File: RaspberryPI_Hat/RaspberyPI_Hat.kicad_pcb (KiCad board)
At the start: 2 copper layers, 65 x 56 mm, 43 parts, among them Q1 BC817, Q2 BC817, Q3 BC817, SW1 SW_PUSH, U1 CAT24C32WI-GT3

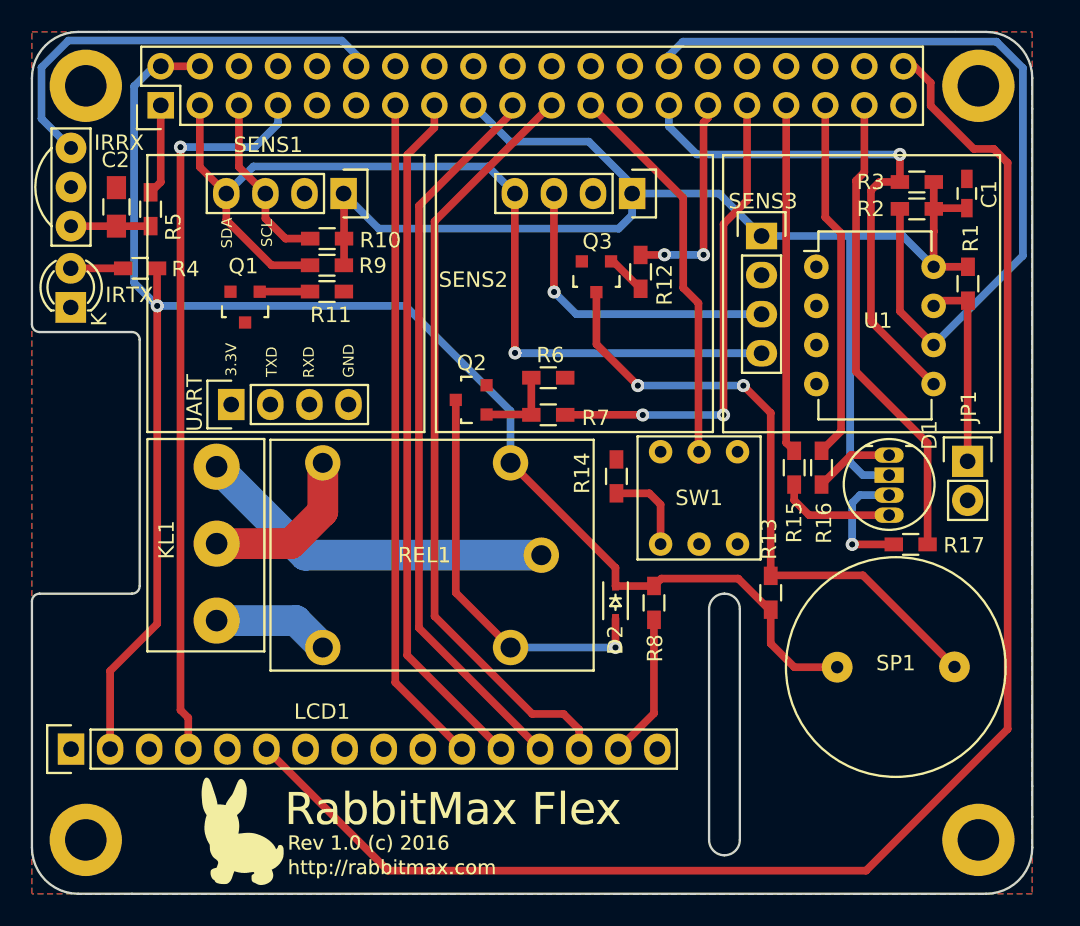
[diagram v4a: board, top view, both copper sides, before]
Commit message: Text on socket's pads
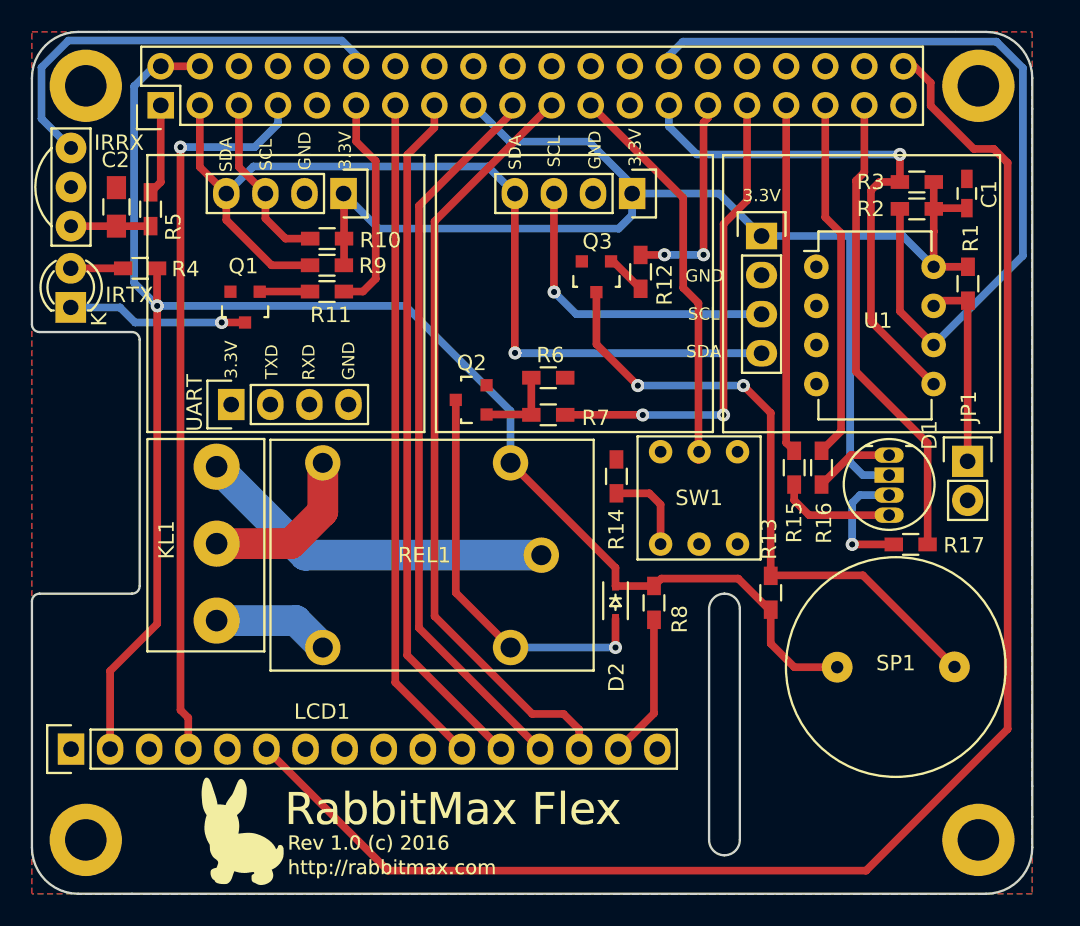
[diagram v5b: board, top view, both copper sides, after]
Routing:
- net Net-(R11-Pad2): track 0.00 -> 14.2 mm
- net Net-(IRTX1-Pad1): track 0.00 -> 11.7 mm, vias 0 -> 1
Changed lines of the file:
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@@
   (general
     (links 102)
-    (no_connects 9)
-    (area 97.924999 68.524999 163.075001 124.675001)
+    (no_connects 7)
+    (area 86.242429 56.842428 174.757572 125.479)
     (thickness 1.6)
-    (drawings 34)
-    (tracks 234)
+    (drawings 44)
+    (tracks 245)
     (zones 0)
     (modules 43)
@@
     (40 Dwgs.User user)
     (41 Cmts.User user)
-    (42 Eco1.User user)
-    (43 Eco2.User user)
+    (42 Eco1.User user hide)
+    (43 Eco2.User user hide)
     (44 Edge.Cuts user)
     (45 Margin user)
@@
     (visible_elements 7FFEEE7F)
     (pcbplotparams
-      (layerselection 0x00030_80000001)
+      (layerselection 0x010e0_80000001)
       (usegerberextensions false)
       (excludeedgelayer true)
@@
     (descr "Through hole pin header")
     (tags "pin header")
-    (fp_text reference SENS2 (at 8.1 15.57 360) (layer F.SilkS)
+    (fp_text reference SENS2 (at 8.1 15.57 360) (layer F.SilkS) hide
       (effects (font (size 1 1) (thickness 0.15)))
     )
@@
     (descr "Through hole pin header")
     (tags "pin header")
-    (fp_text reference SENS1 (at -0.66 10.15 360) (layer F.SilkS)
+    (fp_text reference SENS1 (at -0.66 10.15 360) (layer F.SilkS) hide
       (effects (font (size 1 1) (thickness 0.15)))
     )
@@
     (tags SOD-323)
     (attr smd)
-    (fp_text reference D2 (at 2.45 0.01 270) (layer F.SilkS)
+    (fp_text reference D2 (at 4.87 -0.06 270) (layer F.SilkS)
       (effects (font (size 1 1) (thickness 0.15)))
     )
@@
     (tags "resistor 0603")
     (attr smd)
-    (fp_text reference R8 (at -2.95 0.07 270) (layer F.SilkS)
+    (fp_text reference R8 (at -1.06 1.67 270) (layer F.SilkS)
       (effects (font (size 1 1) (thickness 0.15)))
     )
@@
     (tags "resistor 0603")
     (attr smd)
-    (fp_text reference R14 (at 0.21 -2.23 90) (layer F.SilkS)
+    (fp_text reference R14 (at -3.45 0 90) (layer F.SilkS)
       (effects (font (size 1 1) (thickness 0.15)))
     )
@@
     (descr "Through hole pin header")
     (tags "pin header")
-    (fp_text reference SENS3 (at 2.59 2.99) (layer F.SilkS)
+    (fp_text reference SENS3 (at 2.59 2.99) (layer F.SilkS) hide
       (effects (font (size 1 1) (thickness 0.15)))
     )
@@
     )
   )
-  (gr_text SDA (at 110.67 81.66 90) (layer F.SilkS)
-    (effects (font (size 0.7 0.7) (thickness 0.1)))
-  )
-  (gr_text SCL (at 113.27 81.67 90) (layer F.SilkS)
-    (effects (font (size 0.7 0.7) (thickness 0.1)))
+  (gr_text SCL (at 141.65 86.93) (layer F.SilkS)
+    (effects (font (size 0.8 0.8) (thickness 0.1)))
+  )
+  (gr_text SDA (at 141.65 89.37) (layer F.SilkS)
+    (effects (font (size 0.8 0.8) (thickness 0.1)))
+  )
+  (gr_text SDA (at 129.4 76.42 90) (layer F.SilkS)
+    (effects (font (size 0.8 0.8) (thickness 0.1)))
+  )
+  (gr_text SCL (at 131.93 76.36 90) (layer F.SilkS)
+    (effects (font (size 0.8 0.8) (thickness 0.1)))
+  )
+  (gr_text GND (at 141.71 84.45) (layer F.SilkS)
+    (effects (font (size 0.8 0.8) (thickness 0.1)))
+  )
+  (gr_text GND (at 134.58 76.27 90) (layer F.SilkS)
+    (effects (font (size 0.8 0.8) (thickness 0.1)))
+  )
+  (gr_text 3.3V (at 145.42 79.23) (layer F.SilkS)
+    (effects (font (size 0.8 0.8) (thickness 0.1)))
+  )
+  (gr_text 3.3V (at 137.19 76.11 90) (layer F.SilkS)
+    (effects (font (size 0.8 0.8) (thickness 0.1)))
+  )
+  (gr_text 3.3V (at 118.35 76.3 90) (layer F.SilkS)
+    (effects (font (size 0.8 0.8) (thickness 0.1)))
+  )
+  (gr_text GND (at 115.73 76.33 90) (layer F.SilkS)
+    (effects (font (size 0.8 0.8) (thickness 0.1)))
+  )
+  (gr_text SDA (at 110.61 76.56 90) (layer F.SilkS)
+    (effects (font (size 0.8 0.8) (thickness 0.1)))
+  )
+  (gr_text SCL (at 113.21 76.58 90) (layer F.SilkS)
+    (effects (font (size 0.8 0.8) (thickness 0.1)))
   )
   (gr_text GND (at 118.58 89.97 90) (layer F.SilkS)
-    (effects (font (size 0.7 0.7) (thickness 0.1)))
+    (effects (font (size 0.8 0.8) (thickness 0.1)))
   )
   (gr_text 3.3V (at 110.95 89.89 90) (layer F.SilkS)
-    (effects (font (size 0.7 0.7) (thickness 0.1)))
+    (effects (font (size 0.8 0.8) (thickness 0.1)))
   )
   (gr_text TXD (at 113.58 90.03 90) (layer F.SilkS)
-    (effects (font (size 0.7 0.7) (thickness 0.1)))
+    (effects (font (size 0.8 0.8) (thickness 0.1)))
   )
   (gr_text RXD (at 115.99 90.06 90) (layer F.SilkS)
-    (effects (font (size 0.7 0.7) (thickness 0.1)))
+    (effects (font (size 0.8 0.8) (thickness 0.1)))
   )
   (gr_line (start 105 88.6) (end 105 104.6) (angle 90) (layer Edge.Cuts) (width 0.15))
@@
   (segment (start 111.45 73.37) (end 111.45 77.38) (width 0.5) (layer F.Cu) (net 31))
   (segment (start 111.45 77.38) (end 113.17 79.1) (width 0.5) (layer F.Cu) (net 31))
+  (segment (start 119.07 73.37) (end 119.07 75.72) (width 0.5) (layer F.Cu) (net 32))
+  (segment (start 119.51 85.47) (end 118.27 85.47) (width 0.5) (layer F.Cu) (net 32))
+  (segment (start 120.34 84.64) (end 119.51 85.47) (width 0.5) (layer F.Cu) (net 32))
+  (segment (start 120.34 76.99) (end 120.34 84.64) (width 0.5) (layer F.Cu) (net 32))
+  (segment (start 119.07 75.72) (end 120.34 76.99) (width 0.5) (layer F.Cu) (net 32))
   (segment (start 141.93 73.37) (end 141.93 74.19) (width 0.5) (layer F.Cu) (net 33))
   (segment (start 141.93 74.19) (end 141.64 74.48) (width 0.5) (layer F.Cu) (net 33))
@@
   (segment (start 119.07 70.83) (end 119.07 70.09) (width 0.5) (layer B.Cu) (net 50))
   (segment (start 119.07 70.09) (end 118.14 69.16) (width 0.5) (layer B.Cu) (net 50))
+  (segment (start 111.85 87.47822) (end 110.33178 87.47822) (width 0.5) (layer F.Cu) (net 51))
+  (segment (start 103.72 86.5) (end 100.52 86.5) (width 0.5) (layer B.Cu) (net 51))
+  (segment (start 104.7 87.48) (end 103.72 86.5) (width 0.5) (layer B.Cu) (net 51))
+  (segment (start 110.33 87.48) (end 104.7 87.48) (width 0.5) (layer B.Cu) (net 51))
+  (via (at 110.33 87.48) (size 0.85) (drill 0.4) (layers F.Cu B.Cu) (net 51))
+  (segment (start 110.33178 87.47822) (end 110.33 87.48) (width 0.5) (layer F.Cu) (net 51))
   (segment (start 100.52 83.96) (end 103.93 83.96) (width 0.5) (layer F.Cu) (net 52))
   (zone (net 1) (net_name GND) (layer F.Cu) (hatch edge 0.508)

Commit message: Changed to 5 I2C sensors on headers
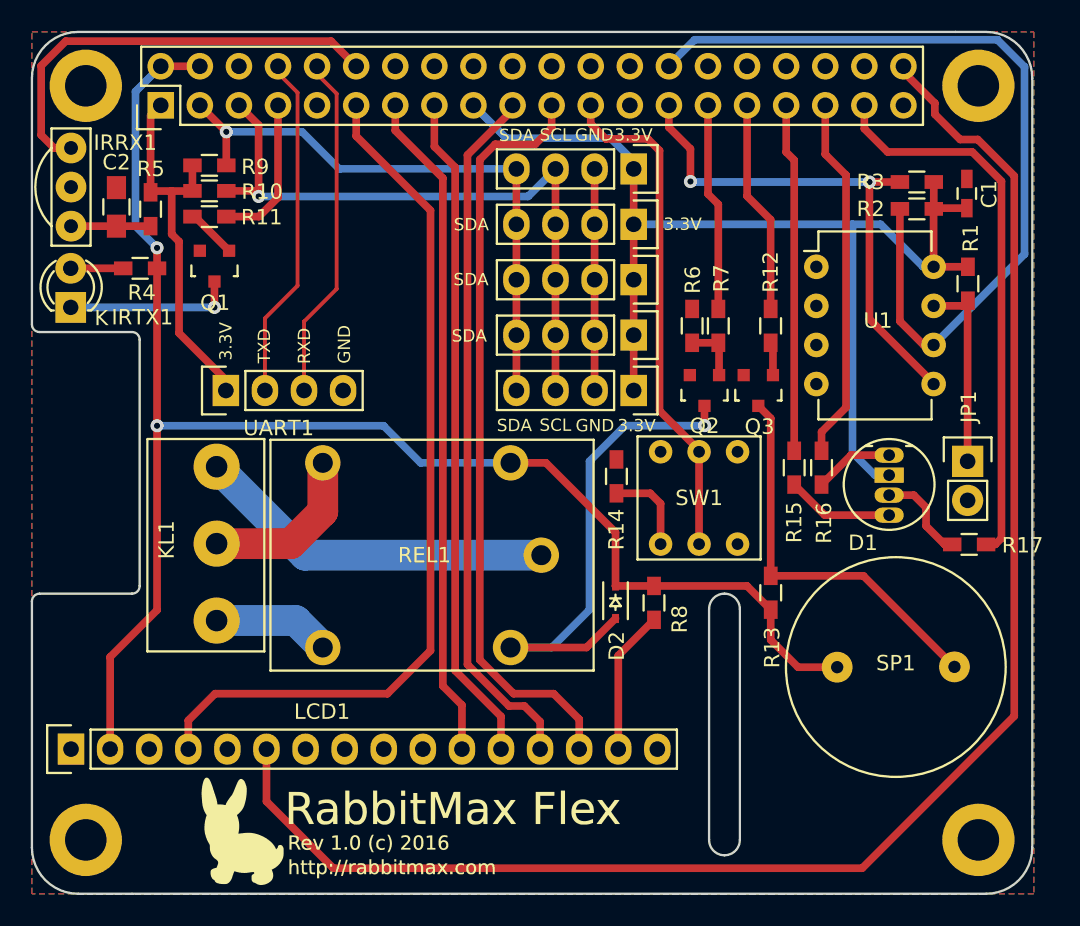
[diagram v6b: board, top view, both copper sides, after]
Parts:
- added SENS4: I2C_SENS_1, Pin_Headers:Pin_Header_Straight_1x04, F.Cu at (137.1, 91.9)
- added SENS5: I2C_SENS_1, Pin_Headers:Pin_Header_Straight_1x04, F.Cu at (137.1, 77.5)
- SENS1, SENS2, SENS3: footprint myfootprint:I2C_SENS_1 -> Pin_Headers:Pin_Header_Straight_1x04
- moved SENS1 17.9 mm to (137.1, 88.3)
- moved Q2 15.2 mm to (141.7, 91.9), turned to 180 degrees
- moved Q3 12.9 mm to (145.2, 91.9)
- moved R7 12.5 mm to (142.6, 87.7), turned to 90 degrees
- moved R9 10.0 mm to (109.5, 77.3), turned to 0 degrees
- moved R6 9.94 mm to (140.9, 87.7), turned to 270 degrees
- moved SENS2 9.60 mm to (137.1, 84.7)
- moved R12 9.15 mm to (146.0, 87.7)
- moved R11 9.06 mm to (109.5, 80.6)
- moved R10 8.25 mm to (109.5, 78.9), turned to 0 degrees
- moved SENS3 7.34 mm to (137.1, 81.1), turned to 270 degrees
- moved R17 3.80 mm to (158.9, 101.9)
- moved Q1 3.32 mm to (109.9, 83.8)
- moved UART1 0.97 mm to (110.6, 91.9)
- renumbered IRRX to IRRX1, IRTX to IRTX1, UART to UART1
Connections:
- RASP_CONN1 pad 11: Net-(R11-Pad2) -> /RS
- RASP_CONN1 pad 29: Net-(R12-Pad2) -> Net-(R7-Pad2)
- RASP_CONN1 pad 31: Net-(R7-Pad2) -> Net-(R12-Pad2)
- RASP_CONN1 pad 7: /RS -> Net-(R11-Pad2)
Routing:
- net /TXD: track 0.33 -> 23.7 mm
- net Net-(R9-Pad2): track 61.4 -> 38.9 mm
- net /RXD: track 0.27 -> 22.5 mm
- net Net-(R7-Pad2): track 31.0 -> 13.5 mm, vias 2 -> 0
- net Net-(Q3-Pad3): track 41.5 -> 25.8 mm, vias 2 -> 0
- net GND: track 0.00 -> 14.4 mm
- net Net-(R10-Pad2): track 32.0 -> 43.1 mm
- net /RS: track 47.5 -> 56.9 mm, vias 1 -> 0
- net +5V: track 110.8 -> 103.3 mm, vias 1 -> 2
- net Net-(RASP_CONN1-Pad23): track 26.0 -> 33.1 mm
- net Net-(D2-Pad2): track 26.3 -> 33.1 mm
- net /LED3: track 30.7 -> 36.2 mm
- net +3V3: track 94.9 -> 99.9 mm
- net Net-(R11-Pad2): track 14.2 -> 9.86 mm
- net /D6: track 47.7 -> 45.6 mm
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
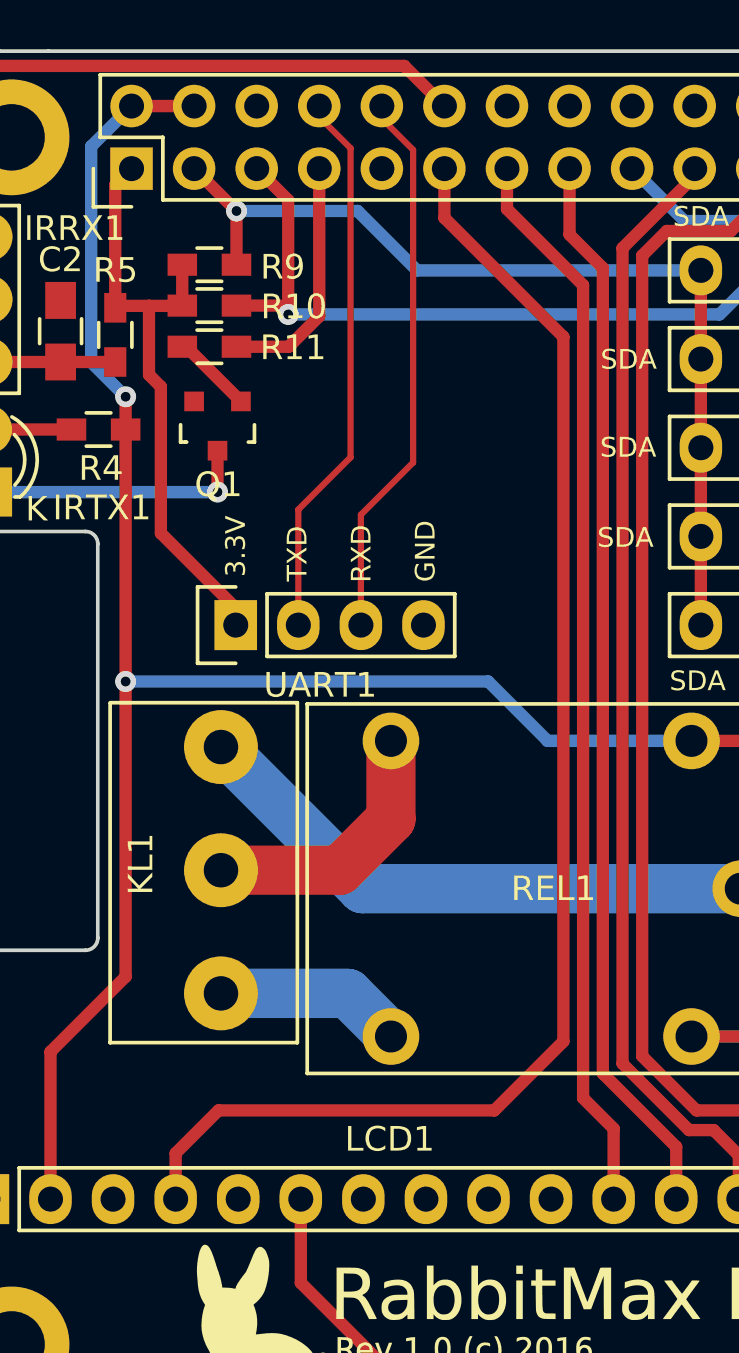
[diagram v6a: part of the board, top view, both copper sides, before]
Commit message: changed IRRT to pin 11 RS to pin 7
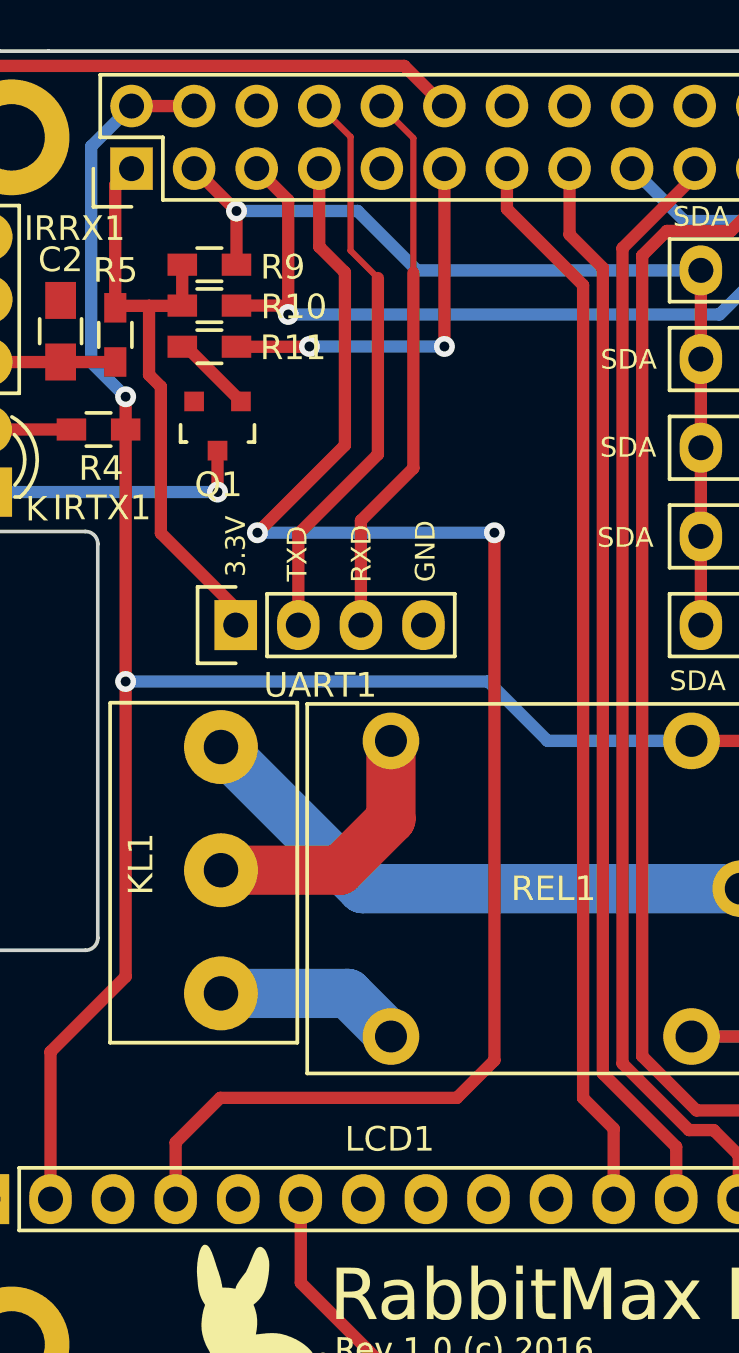
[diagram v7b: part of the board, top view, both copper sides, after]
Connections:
- RASP_CONN1 pad 11: /RS -> Net-(R11-Pad2)
- RASP_CONN1 pad 7: Net-(R11-Pad2) -> /RS
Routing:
- net /RS: track 56.9 -> 64.3 mm, vias 0 -> 2
- net Net-(R11-Pad2): track 9.86 -> 15.7 mm, vias 0 -> 2
